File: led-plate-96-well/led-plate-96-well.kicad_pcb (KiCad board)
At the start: 4 copper layers, 156.8 x 110.7 mm, 121 parts, among them J1 RAPC722X, U1 A000053, U2 TLC5947RHB, U3 TLC5947RHB, U4 TLC5947RHB, U5 TLC5947RHB

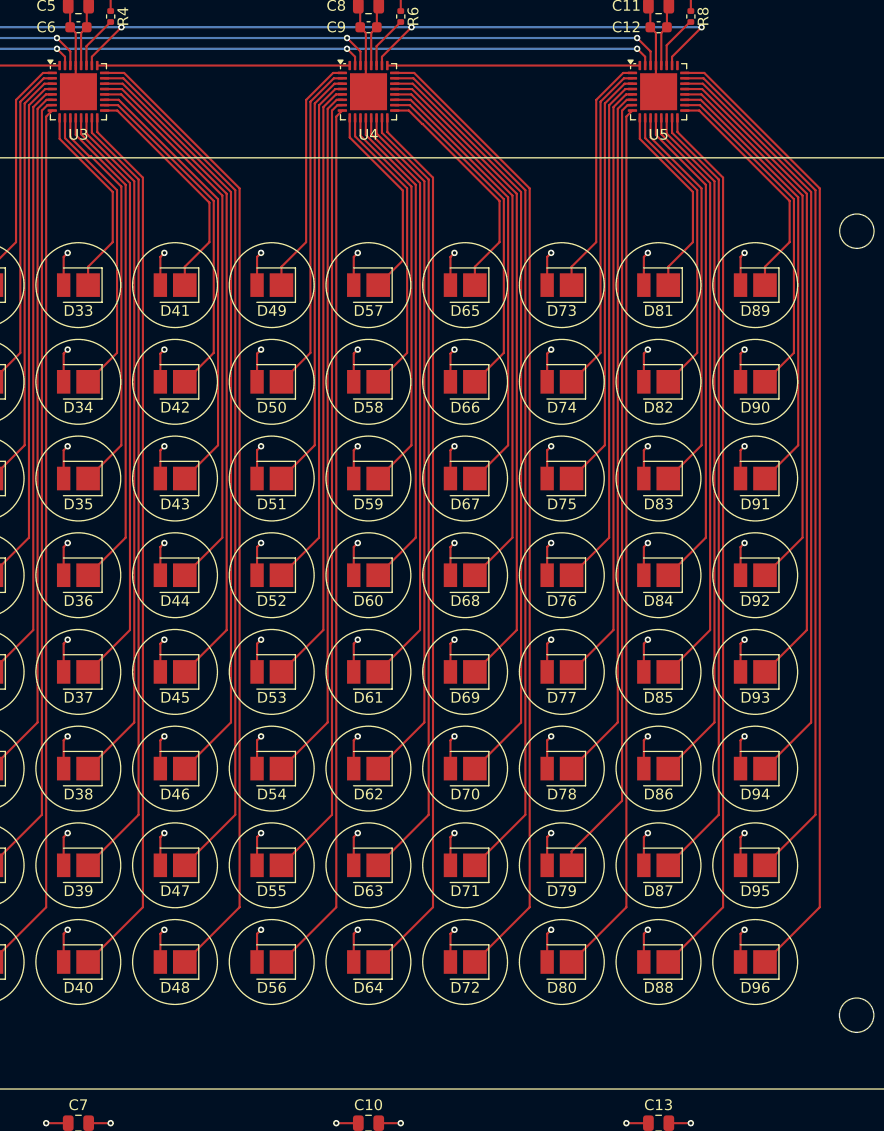
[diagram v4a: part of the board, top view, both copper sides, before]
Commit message: assign parts and fix led driver vias
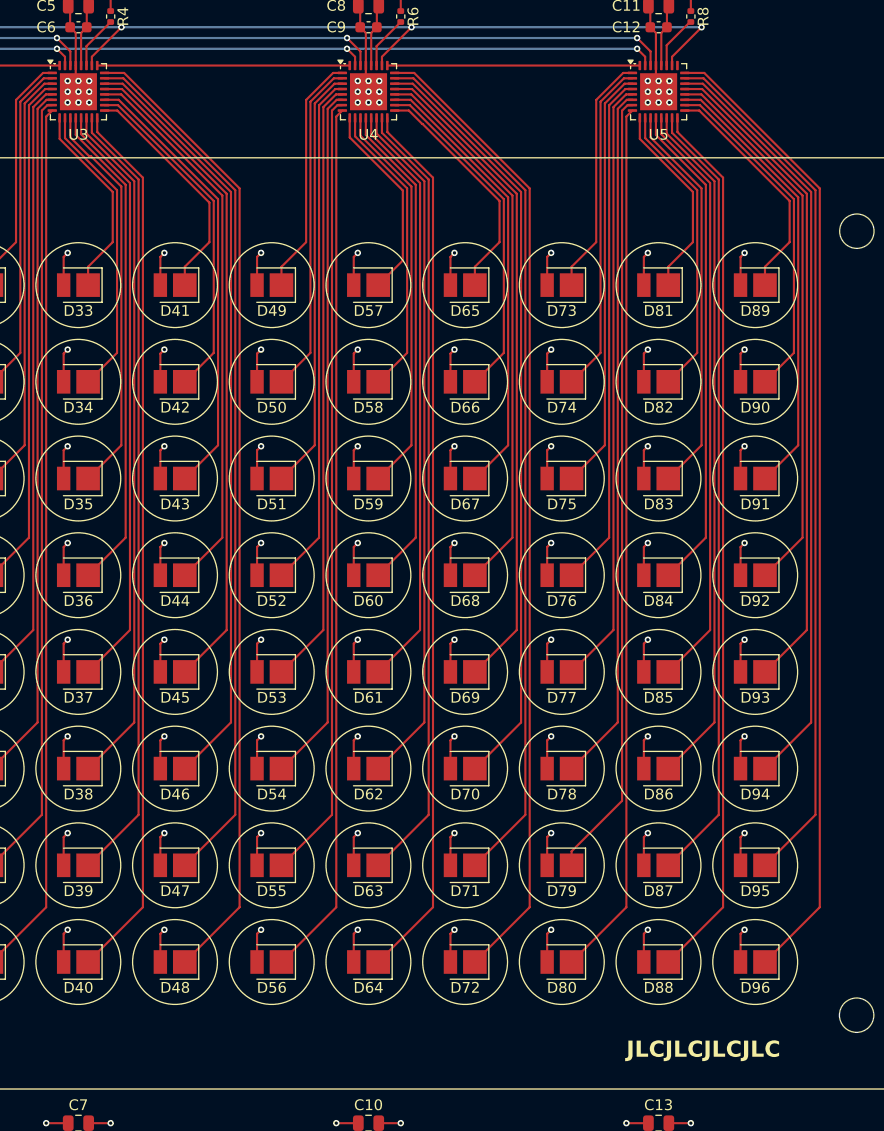
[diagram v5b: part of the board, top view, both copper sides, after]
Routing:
- net GND: track 69.7 -> 105.7 mm, vias 22 -> 49
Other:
- board text added: "JLCJLCJLCJLC"
